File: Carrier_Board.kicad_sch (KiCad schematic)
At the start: 6 parts

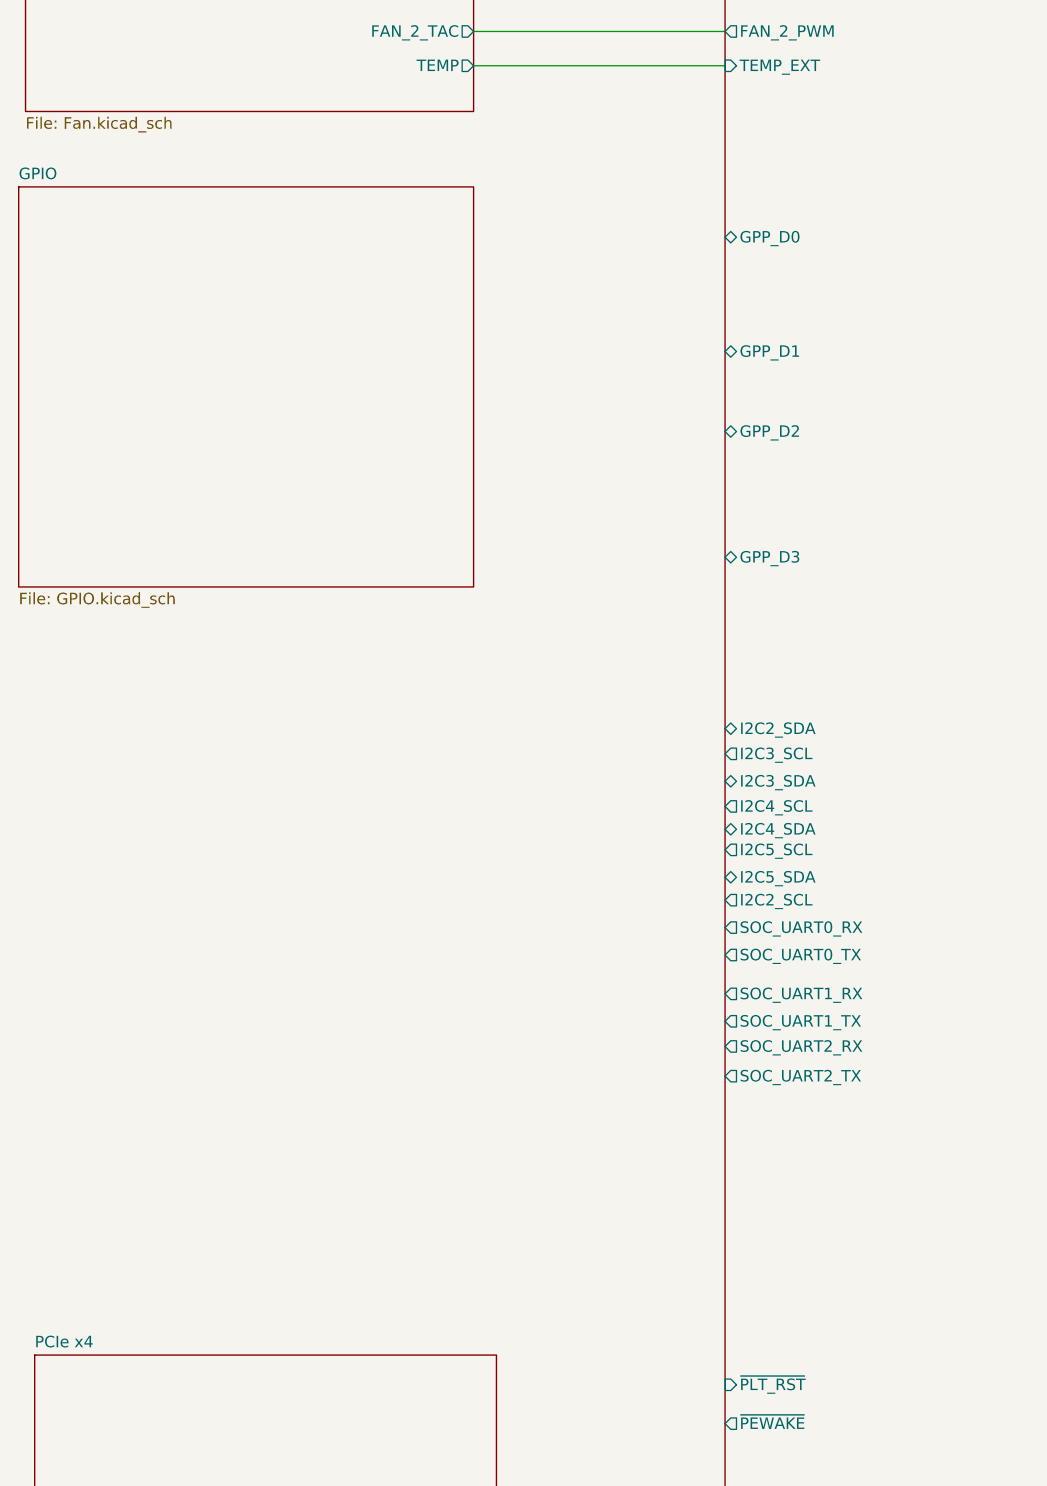
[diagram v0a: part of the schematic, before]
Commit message: Adde the sub sheet schematic for the GPIO and connected the Hierchal sheets together
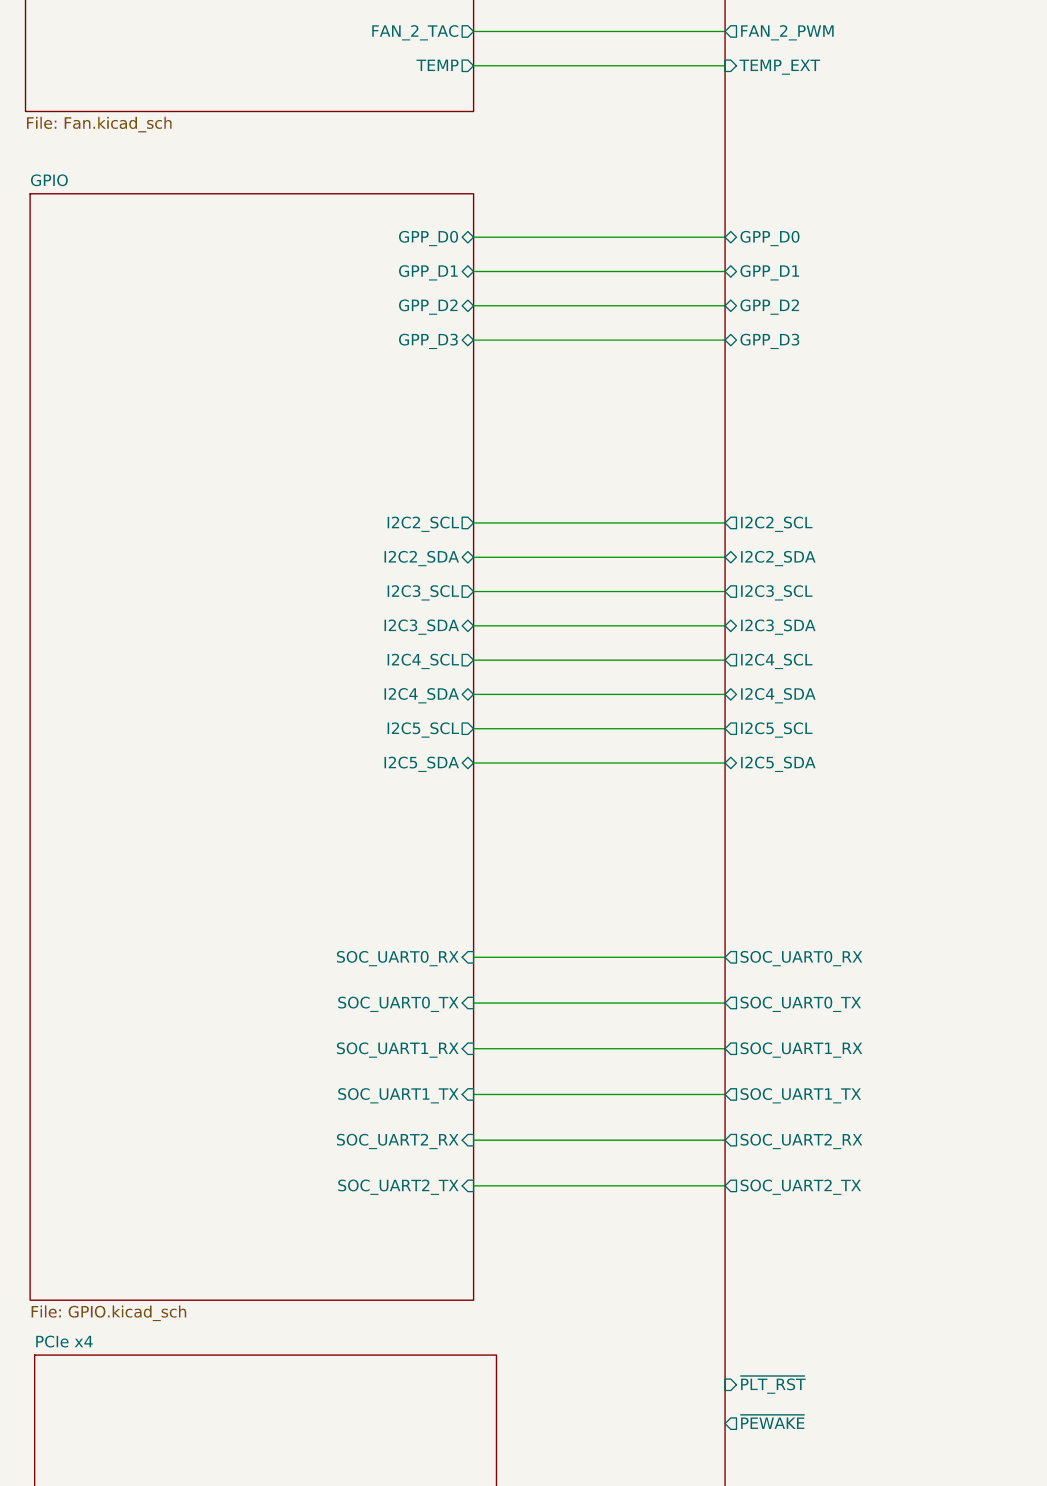
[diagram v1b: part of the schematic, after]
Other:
- sheet GPIO ports: added GPP_D0, GPP_D1, GPP_D2, GPP_D3, I2C2_SCL, I2C2_SDA, I2C3_SCL, I2C3_SDA, I2C4_SCL, I2C4_SDA, I2C5_SCL, I2C5_SDA, SOC_UART0_RX, SOC_UART0_TX, SOC_UART1_RX, SOC_UART1_TX, SOC_UART2_RX, SOC_UART2_TX; removed none

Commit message: finished the pciex4 implememntation
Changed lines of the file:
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@@
 	)
 	(sheet
-		(at 330.2 75.438)
+		(at 328.93 80.518)
 		(size 38.354 37.592)
 		(exclude_from_sim no)
@@
 		)
 		(property "Sheetname" "Gigabit Ethernet"
-			(at 330.2 74.7264 0)
+			(at 328.93 79.8064 0)
 			(show_name no)
 			(do_not_autoplace no)
@@
 		)
 		(property "Sheetfile" "ethernet.kicad_sch"
-			(at 330.2 113.6146 0)
+			(at 328.93 118.6946 0)
 			(show_name no)
 			(do_not_autoplace no)
@@
 	)
 	(sheet
-		(at 126.492 289.306)
-		(size 51.308 75.692)
+		(at 125.73 288.925)
+		(size 49.53 76.073)
 		(exclude_from_sim no)
 		(in_bom yes)
@@
 		)
 		(property "Sheetname" "PCIe x4"
-			(at 126.492 288.5944 0)
+			(at 125.73 288.2134 0)
 			(show_name no)
 			(do_not_autoplace no)
@@
 		)
 		(property "Sheetfile" "pciex4.kicad_sch"
-			(at 126.492 365.5826 0)
+			(at 125.73 365.5826 0)
 			(show_name no)
 			(do_not_autoplace no)
@@
 	)
 	(sheet
-		(at 125.476 123.825)
-		(size 49.784 27.305)
+		(at 125.73 123.825)
+		(size 49.53 27.305)
 		(exclude_from_sim no)
 		(in_bom yes)
@@
 		)
 		(property "Sheetname" "Fan"
-			(at 125.476 123.1134 0)
+			(at 125.73 123.1134 0)
 			(show_name no)
 			(do_not_autoplace no)
@@
 		)
 		(property "Sheetfile" "Fan.kicad_sch"
-			(at 125.476 151.7146 0)
+			(at 125.73 151.7146 0)
 			(show_name no)
 			(do_not_autoplace no)
@@
 	)
 	(sheet
-		(at 125.984 160.274)
-		(size 49.276 122.936)
+		(at 125.73 160.274)
+		(size 49.53 122.936)
 		(exclude_from_sim no)
 		(in_bom yes)
@@
 		)
 		(property "Sheetname" "GPIO"
-			(at 125.984 159.5624 0)
+			(at 125.73 159.5624 0)
 			(show_name no)
 			(do_not_autoplace no)
@@
 		)
 		(property "Sheetfile" "GPIO.kicad_sch"
-			(at 125.984 283.7946 0)
+			(at 125.73 283.7946 0)
 			(show_name no)
 			(do_not_autoplace no)
@@
 	)
 	(sheet
-		(at 329.692 152.654)
+		(at 329.692 151.384)
 		(size 42.672 75.692)
 		(exclude_from_sim no)
@@
 		)
 		(property "Sheetname" "USB 2.0 & 3.0"
-			(at 329.692 151.9424 0)
+			(at 329.692 150.6724 0)
 			(show_name no)
 			(do_not_autoplace no)
@@
 		)
 		(property "Sheetfile" "usb_2_3.kicad_sch"
-			(at 329.692 228.9306 0)
-			(show_name no)
-			(do_not_autoplace no)
+			(at 329.692 227.6606 0)
+			(show_name no)
+			(do_not_autoplace no)

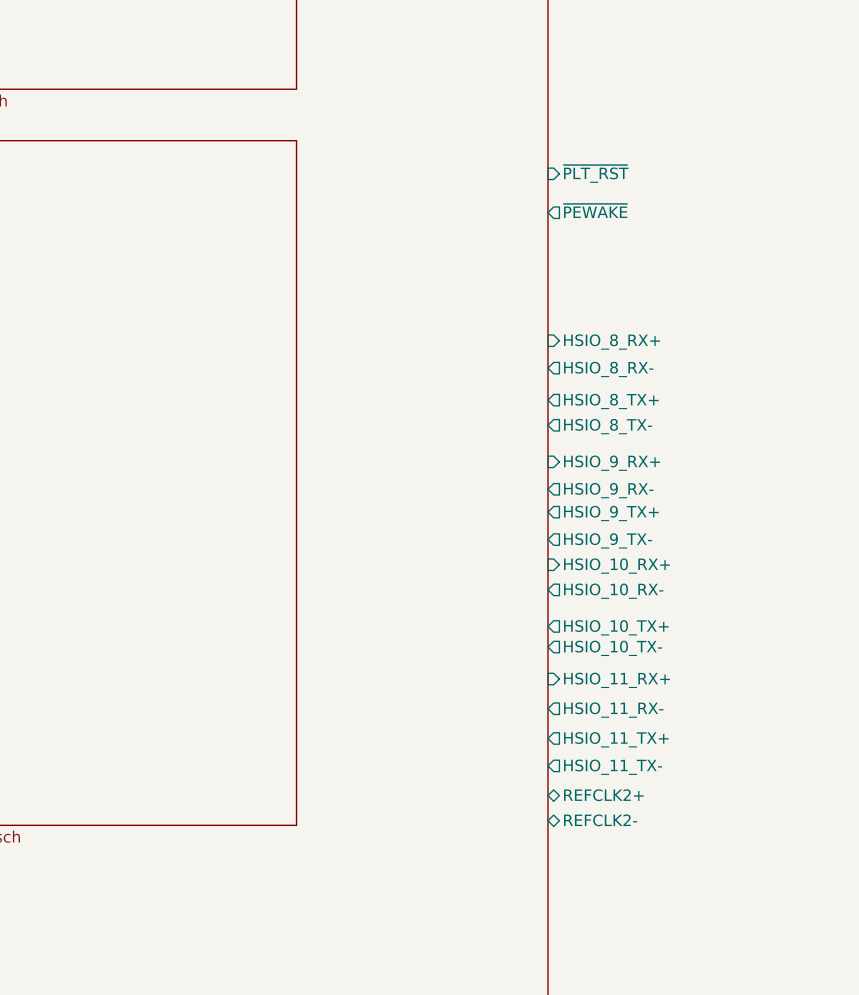
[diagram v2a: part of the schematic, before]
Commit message: Connected the hierchal labels to the main mu module in the root sheet
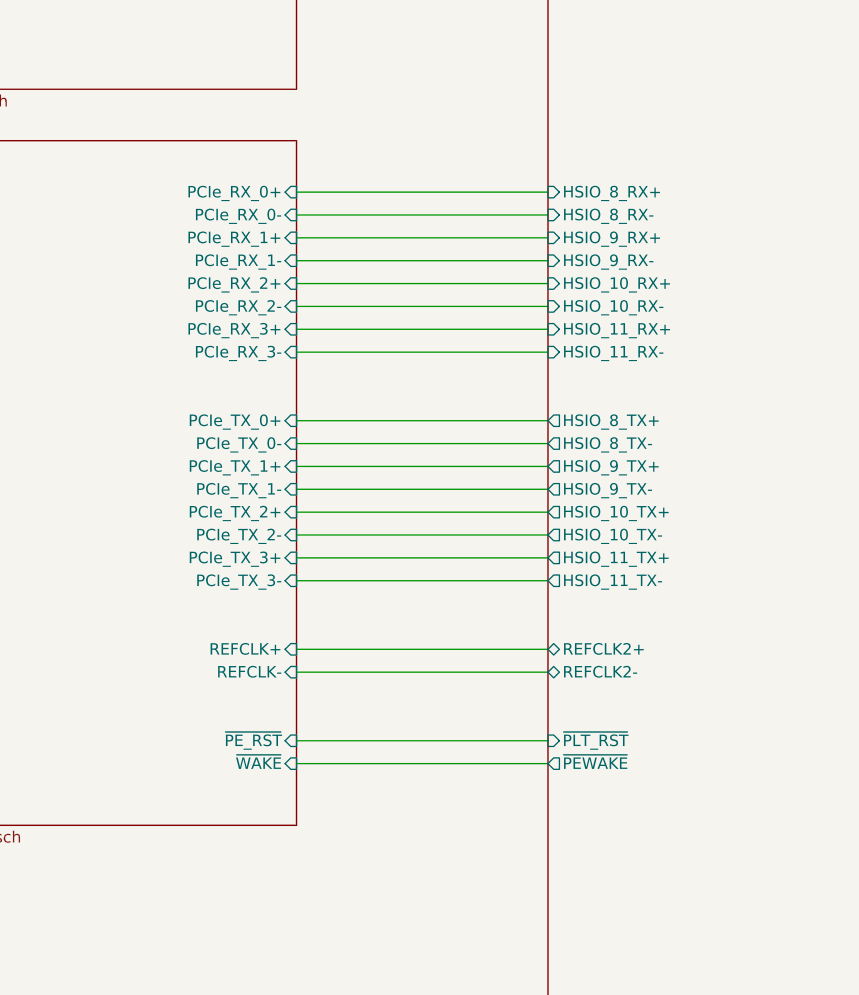
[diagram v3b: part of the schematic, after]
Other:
- sheet PCIe x4 ports: added PCIe_RX_0+, PCIe_RX_0-, PCIe_RX_1+, PCIe_RX_1-, PCIe_RX_2+, PCIe_RX_2-, PCIe_RX_3+, PCIe_RX_3-, PCIe_TX_0+, PCIe_TX_0-, PCIe_TX_1+, PCIe_TX_1-, PCIe_TX_2+, PCIe_TX_2-, PCIe_TX_3+, PCIe_TX_3-, REFCLK+, REFCLK-, ~{PE_RST}, ~{WAKE}; removed none

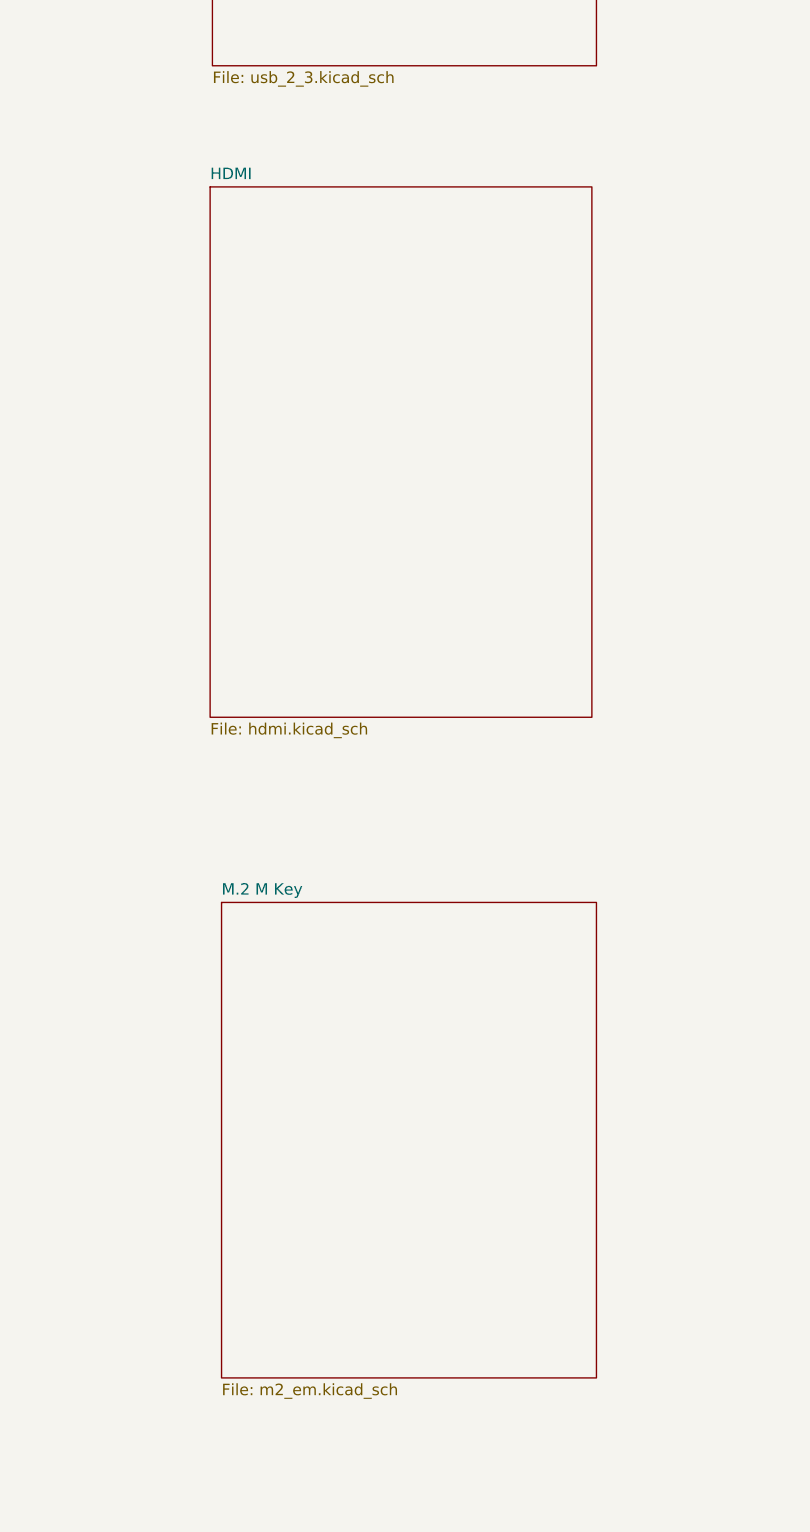
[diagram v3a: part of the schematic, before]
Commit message: Finished part of the M.2. schematic capture
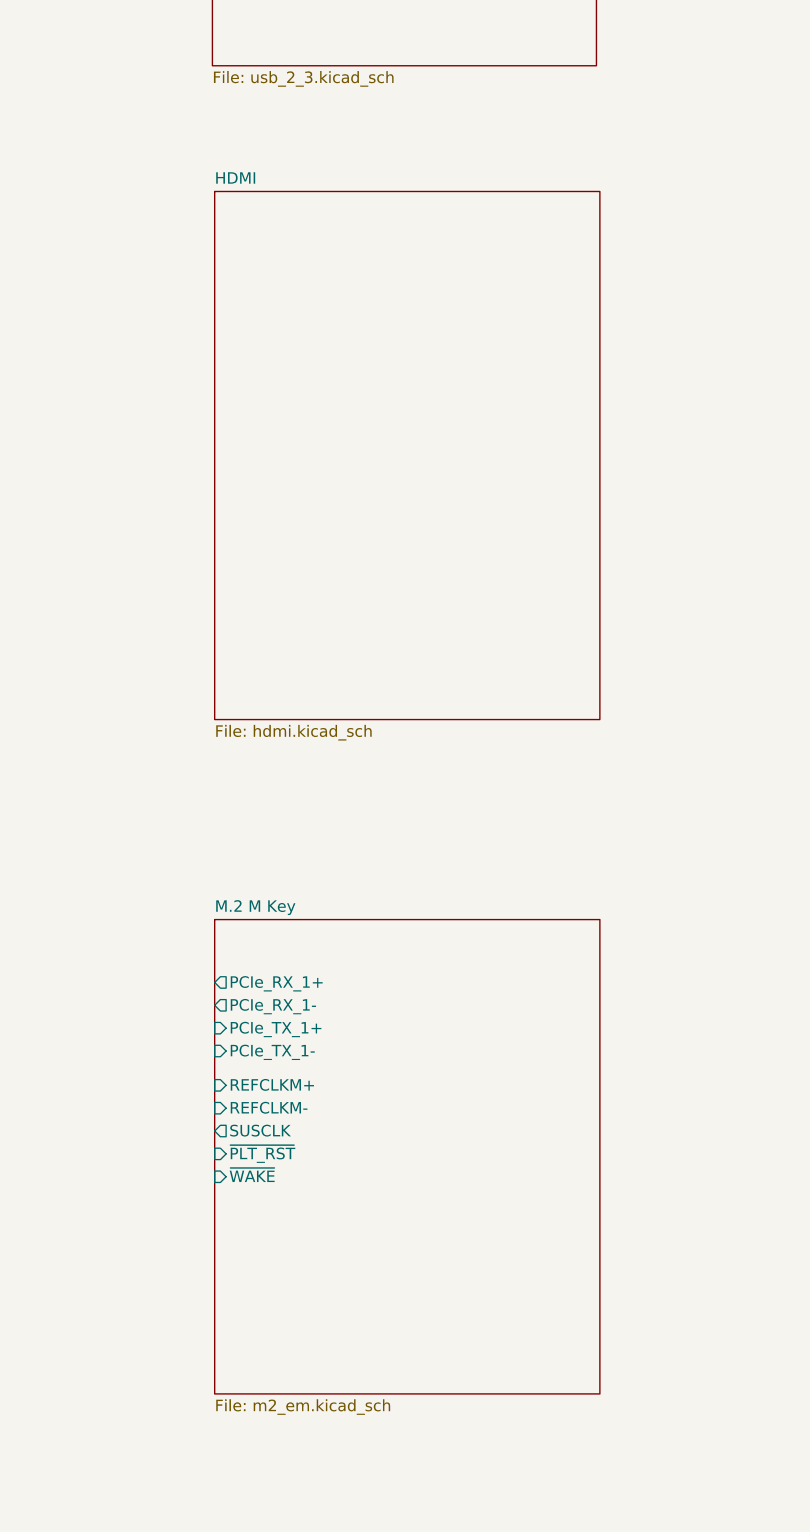
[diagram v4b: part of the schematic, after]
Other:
- sheet M.2 M Key ports: added PCIe_RX_1+, PCIe_RX_1-, PCIe_TX_1+, PCIe_TX_1-, REFCLKM+, REFCLKM-, SUSCLK, ~{PLT_RST}, ~{WAKE}; removed none
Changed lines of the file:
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@@
 	)
 	(sheet
-		(at 329.438 240.538)
-		(size 42.418 58.928)
+		(at 329.946 241.046)
+		(size 42.799 58.674)
 		(exclude_from_sim no)
 		(in_bom yes)
@@
 		)
 		(property "Sheetname" "HDMI"
-			(at 329.438 239.8264 0)
+			(at 329.946 240.3344 0)
 			(show_name no)
 			(do_not_autoplace no)
@@
 		)
 		(property "Sheetfile" "hdmi.kicad_sch"
-			(at 329.438 300.0506 0)
+			(at 329.946 300.3046 0)
 			(show_name no)
 			(do_not_autoplace no)
@@
 	)
 	(sheet
-		(at 330.708 320.04)
-		(size 41.656 52.832)
+		(at 329.946 321.945)
+		(size 42.799 52.705)
 		(exclude_from_sim no)
 		(in_bom yes)
@@
 		)
 		(property "Sheetname" "M.2 M Key"
-			(at 330.708 319.3284 0)
+			(at 329.946 321.2334 0)
 			(show_name no)
 			(do_not_autoplace no)
@@
 		)
 		(property "Sheetfile" "m2_em.kicad_sch"
-			(at 330.708 373.4566 0)
+			(at 329.946 375.2346 0)
 			(show_name no)
 			(do_not_autoplace no)
@@
 			)
 		)
+		(pin "PCIe_RX_1+" output
+			(at 329.946 328.93 180)
+			(effects
+				(font
+					(size 1.27 1.27)
+				)
+				(justify left)
+			)
+		)
+		(pin "PCIe_RX_1-" output
+			(at 329.946 331.47 180)
+			(effects
+				(font
+					(size 1.27 1.27)
+				)
+				(justify left)
+			)
+		)
+		(pin "PCIe_TX_1+" input
+			(at 329.946 334.01 180)
+			(effects
+				(font
+					(size 1.27 1.27)
+				)
+				(justify left)
+			)
+		)
+		(pin "PCIe_TX_1-" input
+			(at 329.946 336.55 180)
+			(effects
+				(font
+					(size 1.27 1.27)
+				)
+				(justify left)
+			)
+		)
+		(pin "REFCLKM+" input
+			(at 329.946 340.36 180)
+			(effects
+				(font
+					(size 1.27 1.27)
+				)
+				(justify left)
+			)
+		)
+		(pin "REFCLKM-" input
+			(at 329.946 342.9 180)
+			(effects
+				(font
+					(size 1.27 1.27)
+				)
+				(justify left)
+			)
+		)
+		(pin "SUSCLK" output
+			(at 329.946 345.44 180)
+			(effects
+				(font
+					(size 1.27 1.27)
+				)
+				(justify left)
+			)
+		)
+		(pin "~{PLT_RST}" input
+			(at 329.946 347.98 180)
+			(effects
+				(font
+					(size 1.27 1.27)
+				)
+				(justify left)
+			)
+		)
+		(pin "~{WAKE}" input
+			(at 329.946 350.52 180)
+			(effects
+				(font
+					(size 1.27 1.27)
+				)
+				(justify left)
+			)
+		)
